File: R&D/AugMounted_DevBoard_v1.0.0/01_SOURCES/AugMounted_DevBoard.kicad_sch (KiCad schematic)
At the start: 1 part

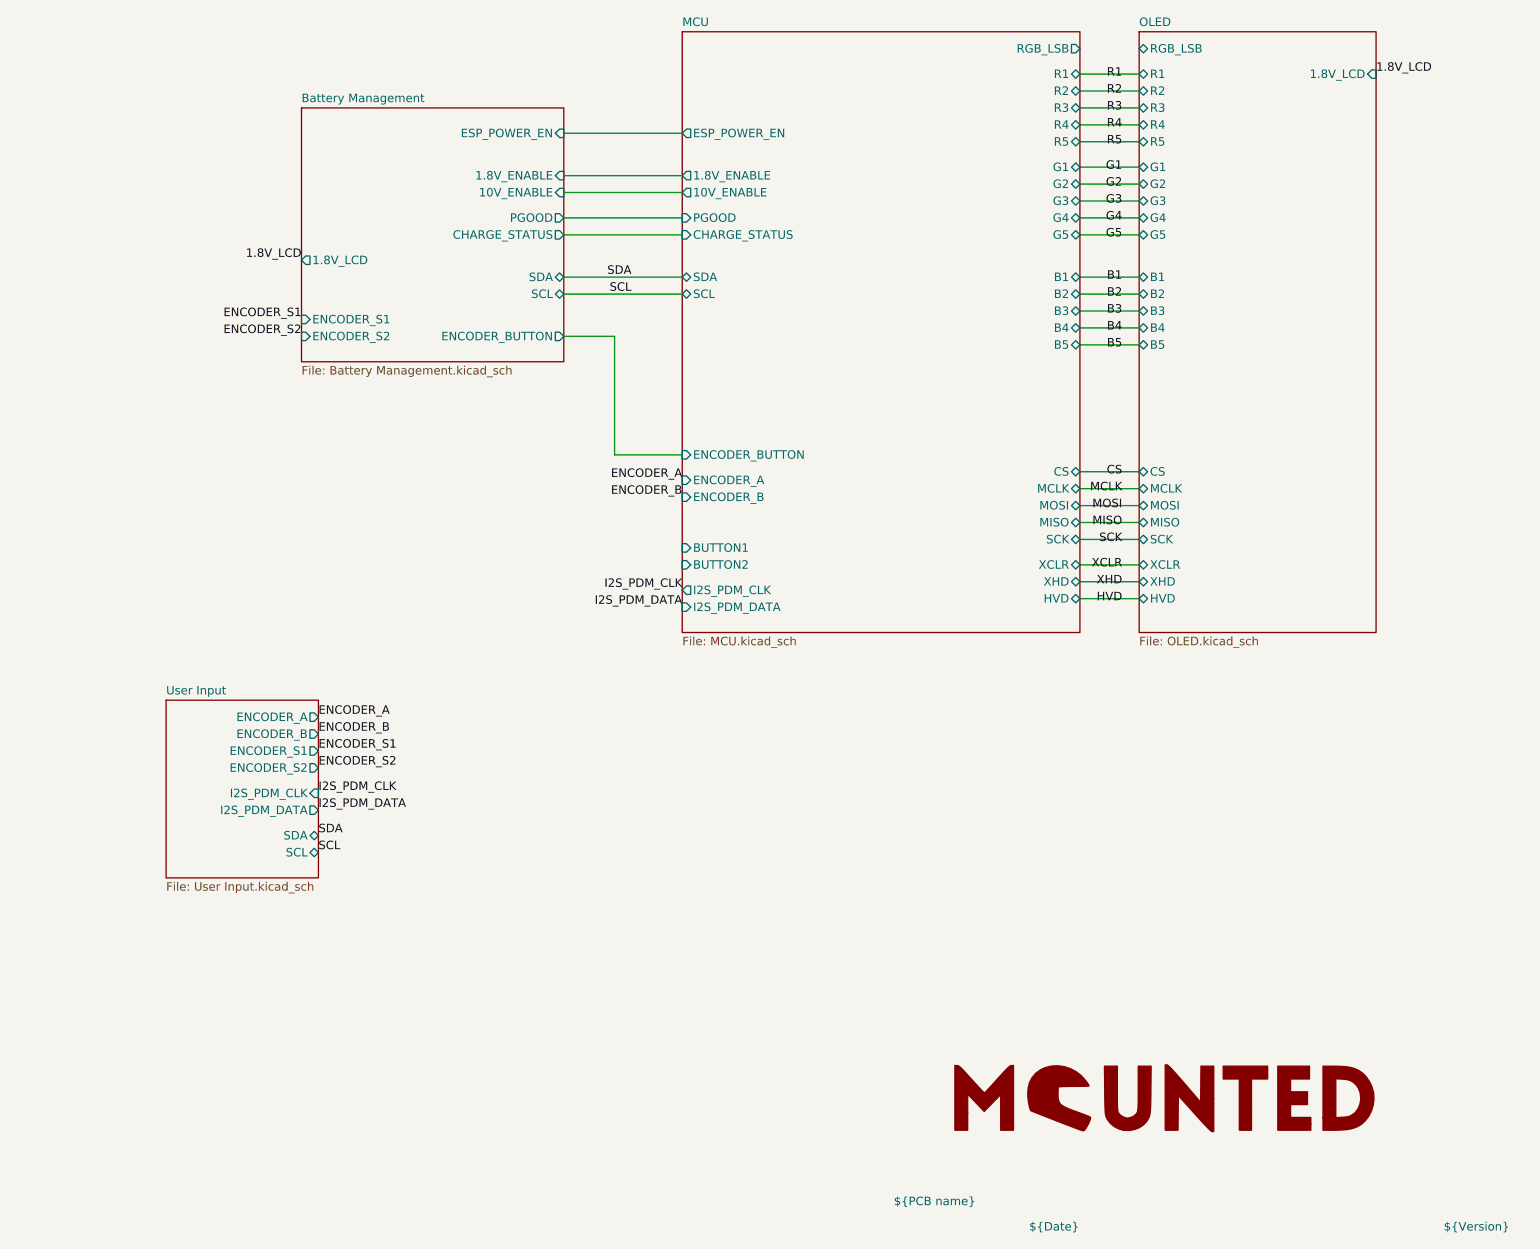
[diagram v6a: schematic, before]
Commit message: Changed layout to a banana shape
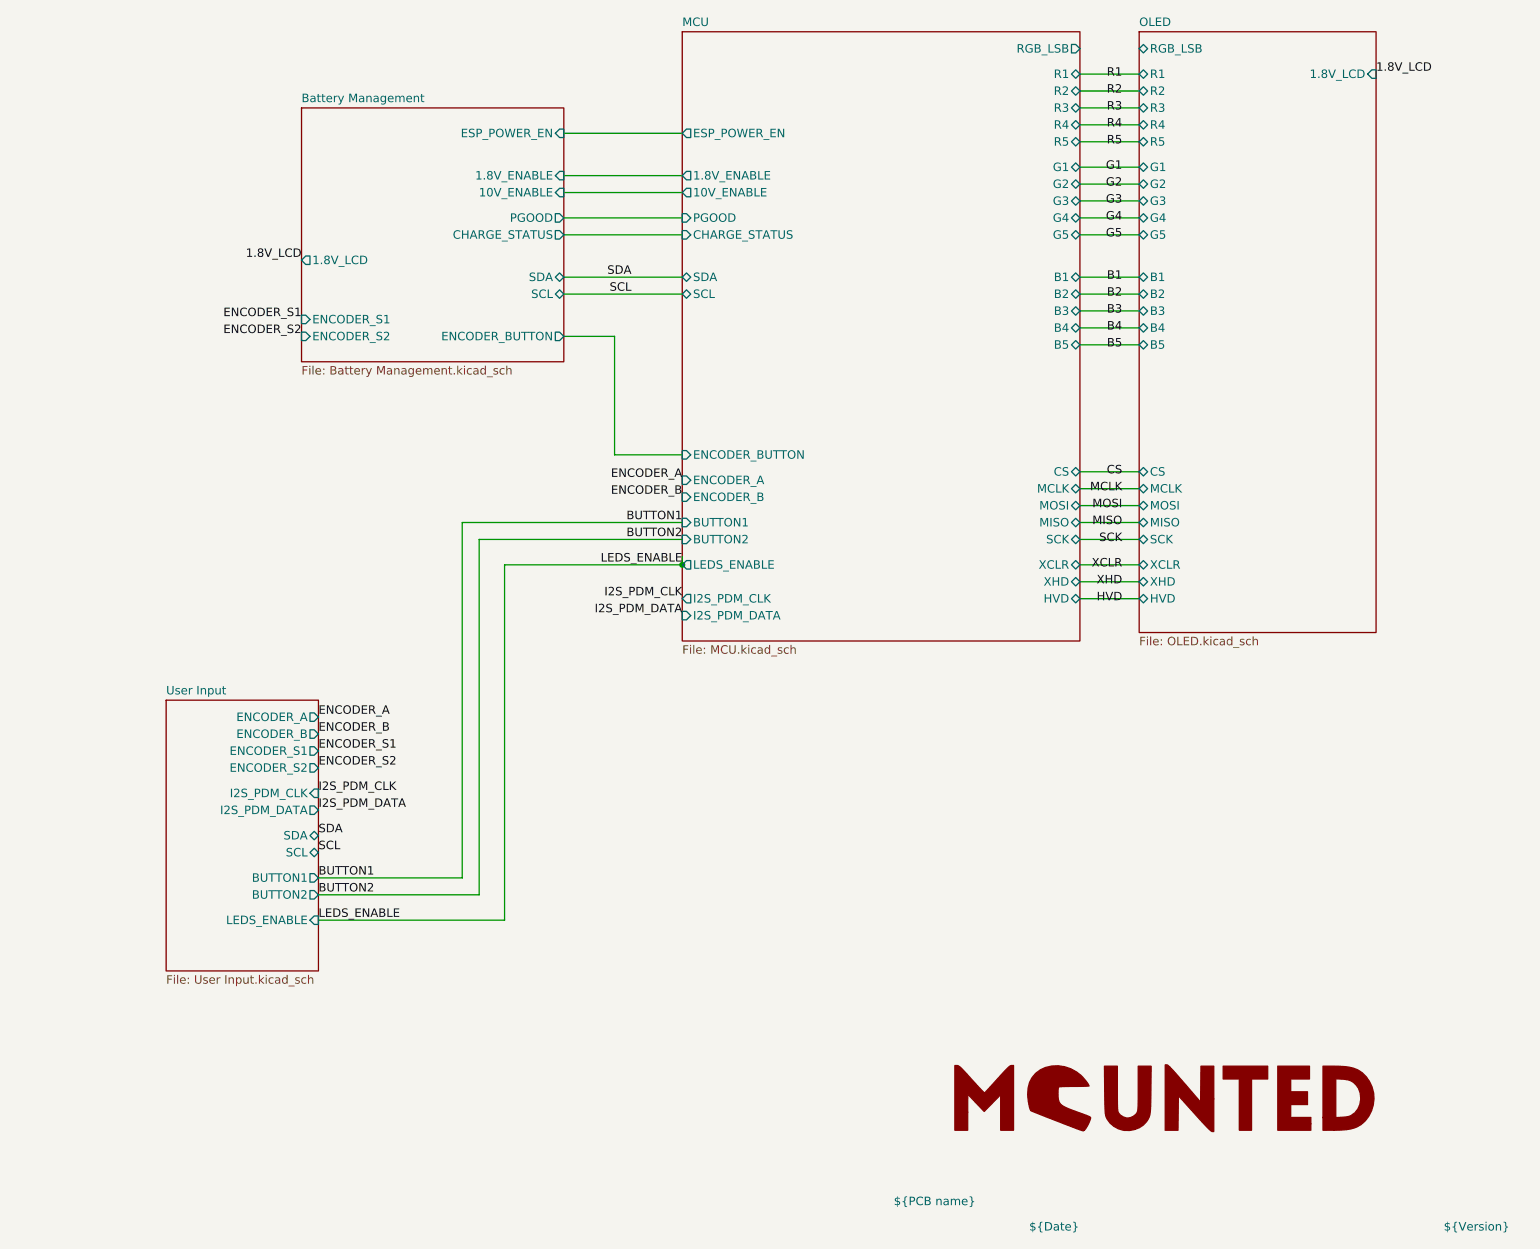
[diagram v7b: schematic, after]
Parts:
- renumbered LOGO1 to LOGO101
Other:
- sheet MCU ports: added LEDS_ENABLE; removed none
- sheet User Input ports: added BUTTON1, BUTTON2, LEDS_ENABLE; removed none
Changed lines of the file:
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@@
 (kicad_sch (version 20230121) (generator eeschema)
   (paper "A4")
+  (junction (at 154.94 93.98) (diameter 0) (color 0 0 0 0)
+  )
   (wire (pts (xy 214.63 55.88) (xy 223.52 55.88))
     (stroke (width 0) (type default))
@@
     (stroke (width 0) (type default))
   )
+  (wire (pts (xy 128.27 93.98) (xy 128.27 147.32))
+    (stroke (width 0) (type default))
+  )
   (wire (pts (xy 214.63 99.06) (xy 223.52 99.06))
     (stroke (width 0) (type default))
@@
     (stroke (width 0) (type default))
   )
+  (wire (pts (xy 154.94 93.98) (xy 128.27 93.98))
+    (stroke (width 0) (type default))
+  )
   (wire (pts (xy 137.16 59.69) (xy 144.78 59.69))
     (stroke (width 0) (type default))
@@
     (stroke (width 0) (type default))
   )
+  (wire (pts (xy 121.92 87.63) (xy 154.94 87.63))
+    (stroke (width 0) (type default))
+  )
   (wire (pts (xy 214.63 87.63) (xy 223.52 87.63))
     (stroke (width 0) (type default))
@@
     (stroke (width 0) (type default))
   )
+  (wire (pts (xy 154.94 93.98) (xy 154.94 92.71))
+    (stroke (width 0) (type default))
+  )
   (wire (pts (xy 214.63 82.55) (xy 223.52 82.55))
     (stroke (width 0) (type default))
@@
     (stroke (width 0) (type default))
   )
+  (wire (pts (xy 100.33 143.51) (xy 124.46 143.51))
+    (stroke (width 0) (type default))
+  )
+  (wire (pts (xy 128.27 147.32) (xy 100.33 147.32))
+    (stroke (width 0) (type default))
+  )
+  (wire (pts (xy 124.46 143.51) (xy 124.46 90.17))
+    (stroke (width 0) (type default))
+  )
   (wire (pts (xy 137.16 44.45) (xy 154.94 44.45))
     (stroke (width 0) (type default))
@@
     (stroke (width 0) (type default))
   )
+  (wire (pts (xy 100.33 140.97) (xy 121.92 140.97))
+    (stroke (width 0) (type default))
+  )
   (wire (pts (xy 144.78 59.69) (xy 144.78 77.47))
     (stroke (width 0) (type default))
@@
     (stroke (width 0) (type default))
   )
+  (wire (pts (xy 121.92 140.97) (xy 121.92 87.63))
+    (stroke (width 0) (type default))
+  )
   (wire (pts (xy 137.16 38.1) (xy 154.94 38.1))
     (stroke (width 0) (type default))
   )
+  (wire (pts (xy 124.46 90.17) (xy 154.94 90.17))
+    (stroke (width 0) (type default))
+  )
   (wire (pts (xy 214.63 41.91) (xy 223.52 41.91))
     (stroke (width 0) (type default))
@@
     (effects (font (size 1.27 1.27)) (justify right))
   )
+  (label "LEDS_ENABLE" (at 154.94 93.98 180) (fields_autoplaced)
+    (effects (font (size 1.27 1.27)) (justify right bottom))
+  )
   (label "ENCODER_S2" (at 97.79 59.69 180) (fields_autoplaced)
     (effects (font (size 1.27 1.27)) (justify right bottom))
@@
     (effects (font (size 1.27 1.27)) (justify right bottom))
   )
-  (label "I2S_PDM_CLK" (at 154.94 97.79 180) (fields_autoplaced)
+  (label "I2S_PDM_CLK" (at 154.94 99.06 180) (fields_autoplaced)
     (effects (font (size 1.27 1.27)) (justify right bottom))
   )
@@
     (effects (font (size 1.27 1.27)) (justify right))
   )
+  (label "BUTTON1" (at 154.94 87.63 180) (fields_autoplaced)
+    (effects (font (size 1.27 1.27)) (justify right bottom))
+  )
   (label "ENCODER_S2" (at 100.33 124.46 0) (fields_autoplaced)
     (effects (font (size 1.27 1.27)) (justify left bottom))
@@
     (effects (font (size 1.27 1.27)) (justify right))
   )
-  (label "I2S_PDM_DATA" (at 154.94 100.33 180) (fields_autoplaced)
-    (effects (font (size 1.27 1.27)) (justify right bottom))
+  (label "I2S_PDM_DATA" (at 154.94 101.6 180) (fields_autoplaced)
+    (effects (font (size 1.27 1.27)) (justify right bottom))
+  )
+  (label "BUTTON1" (at 100.33 140.97 0) (fields_autoplaced)
+    (effects (font (size 1.27 1.27)) (justify left bottom))
   )
   (label "ENCODER_S1" (at 100.33 121.92 0) (fields_autoplaced)
@@
     (effects (font (size 1.27 1.27)) (justify right bottom))
   )
+  (label "LEDS_ENABLE" (at 100.33 147.32 0) (fields_autoplaced)
+    (effects (font (size 1.27 1.27)) (justify left bottom))
+  )
   (label "I2S_PDM_DATA" (at 100.33 130.81 0) (fields_autoplaced)
     (effects (font (size 1.27 1.27)) (justify left bottom))
@@
     (effects (font (size 1.27 1.27)) (justify right bottom))
   )
+  (label "BUTTON2" (at 100.33 143.51 0) (fields_autoplaced)
+    (effects (font (size 1.27 1.27)) (justify left bottom))
+  )
   (label "ENCODER_A" (at 100.33 116.84 0) (fields_autoplaced)
     (effects (font (size 1.27 1.27)) (justify left bottom))
@@
   (label "MCLK" (at 220.98 82.55 180) (fields_autoplaced)
     (effects (font (size 1.27 1.27)) (justify right))
+  )
+  (label "BUTTON2" (at 154.94 90.17 180) (fields_autoplaced)
+    (effects (font (size 1.27 1.27)) (justify right bottom))
   )
   (label "G4" (at 220.98 41.91 180) (fields_autoplaced)
@@
   (symbol (lib_id ".mounted-lib:mounted_logo") (at 227.33 173.99 0) (unit 1)
     (in_bom yes) (on_board yes) (dnp no) (fields_autoplaced)
-    (property "Reference" "LOGO1" (at 227.33 167.64 0)
+    (property "Reference" "LOGO101" (at 227.33 167.64 0)
       (effects (font (size 1.27 1.27)) hide)
     )
@@
       (project "AugMounted_DevBoard"
         (path "/75b08848-9393-425e-a17d-60105119a7b1"
-          (reference "LOGO1") (unit 1)
+          (reference "LOGO101") (unit 1)
         )
       )
     )
   )
-  (sheet (at 77.47 114.3) (size 22.86 26.67) (fields_autoplaced)
+  (sheet (at 77.47 114.3) (size 22.86 40.64) (fields_autoplaced)
     (stroke (width 0.1524) (type solid))
     (fill (color 0 0 0 0.0000))
@@
       (effects (font (size 1.27 1.27)) (justify left bottom))
     )
-    (property "Sheetfile" "User Input.kicad_sch" (at 77.47 141.5546 0)
+    (property "Sheetfile" "User Input.kicad_sch" (at 77.47 155.5246 0)
       (effects (font (size 1.27 1.27)) (justify left top))
     )
@@
     )
     (pin "SCL" bidirectional (at 100.33 137.16 0)
+      (effects (font (size 1.27 1.27)) (justify right))
+    )
+    (pin "BUTTON1" output (at 100.33 140.97 0)
+      (effects (font (size 1.27 1.27)) (justify right))
+    )
+    (pin "BUTTON2" output (at 100.33 143.51 0)
+      (effects (font (size 1.27 1.27)) (justify right))
+    )
+    (pin "LEDS_ENABLE" input (at 100.33 147.32 0)
       (effects (font (size 1.27 1.27)) (justify right))
     )
@@
     )
   )
-  (sheet (at 154.94 13.97) (size 59.69 90.17) (fields_autoplaced)
+  (sheet (at 154.94 13.97) (size 59.69 91.44) (fields_autoplaced)
     (stroke (width 0.1524) (type solid))
     (fill (color 0 0 0 0.0000))
@@
       (effects (font (size 1.27 1.27)) (justify left bottom))
     )
-    (property "Sheetfile" "MCU.kicad_sch" (at 154.94 104.7246 0)
+    (property "Sheetfile" "MCU.kicad_sch" (at 154.94 105.9946 0)
       (effects (font (size 1.27 1.27)) (justify left top))
     )
@@
       (effects (font (size 1.27 1.27)) (justify left))
     )
-    (pin "I2S_PDM_CLK" output (at 154.94 97.79 180)
-      (effects (font (size 1.27 1.27)) (justify left))
-    )
-    (pin "I2S_PDM_DATA" input (at 154.94 100.33 180)
-      (effects (font (size 1.27 1.27)) (justify left))
-    )
-    (pin "BUTTON1" input (at 154.94 91.44 180)
+    (pin "I2S_PDM_CLK" output (at 154.94 99.06 180)
+      (effects (font (size 1.27 1.27)) (justify left))
+    )
+    (pin "I2S_PDM_DATA" input (at 154.94 101.6 180)
+      (effects (font (size 1.27 1.27)) (justify left))
+    )
+    (pin "BUTTON1" input (at 154.94 87.63 180)
       (effects (font (size 1.27 1.27)) (justify left))
     )
@@
       (effects (font (size 1.27 1.27)) (justify left))
     )
-    (pin "BUTTON2" input (at 154.94 93.98 180)
+    (pin "BUTTON2" input (at 154.94 90.17 180)
       (effects (font (size 1.27 1.27)) (justify left))
     )
@@
       (effects (font (size 1.27 1.27)) (justify left))
     )
+    (pin "LEDS_ENABLE" output (at 154.94 93.98 180)
+      (effects (font (size 1.27 1.27)) (justify left))
+    )

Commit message: Added resistors for CC1 and CC2 pins, layout is started on the high part of the board
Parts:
- added H101, H102: MountingHole, MountingHole:MountingHole_2.2mm_M2, symbol Mechanical:MountingHole
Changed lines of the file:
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@@
     (effects (font (size 1.27 1.27)) (justify left bottom))
+  )
+  (symbol (lib_id "Mechanical:MountingHole") (at 229.87 138.43 0) (unit 1)
+    (in_bom yes) (on_board yes) (dnp no) (fields_autoplaced)
+    (property "Reference" "H102" (at 232.41 137.16 0)
+      (effects (font (size 1.27 1.27)) (justify left))
+    )
+    (property "Value" "MountingHole" (at 232.41 139.7 0)
+      (effects (font (size 1.27 1.27)) (justify left))
+    )
+    (property "Footprint" "MountingHole:MountingHole_2.2mm_M2" (at 229.87 138.43 0)
+      (effects (font (size 1.27 1.27)) hide)
+    )
+    (property "Datasheet" "~" (at 229.87 138.43 0)
+      (effects (font (size 1.27 1.27)) hide)
+    )
+    (instances
+      (project "AugMounted_DevBoard"
+        (path "/75b08848-9393-425e-a17d-60105119a7b1"
+          (reference "H102") (unit 1)
+        )
+      )
+    )
   )
   (symbol (lib_id ".mounted-lib:mounted_logo") (at 227.33 173.99 0) (unit 1)
@@
         )
       )
+    )
+  )
+  (symbol (lib_id "Mechanical:MountingHole") (at 209.55 138.43 0) (unit 1)
+    (in_bom yes) (on_board yes) (dnp no) (fields_autoplaced)
+    (property "Reference" "H101" (at 212.09 137.16 0)
+      (effects (font (size 1.27 1.27)) (justify left))
+    )
+    (property "Value" "MountingHole" (at 212.09 139.7 0)
+      (effects (font (size 1.27 1.27)) (justify left))
+    )
+    (property "Footprint" "MountingHole:MountingHole_2.2mm_M2" (at 209.55 138.43 0)
+      (effects (font (size 1.27 1.27)) hide)
+    )
+    (property "Datasheet" "~" (at 209.55 138.43 0)
+      (effects (font (size 1.27 1.27)) hide)
+    )
+    (instances
+      (project "AugMounted_DevBoard"
+        (path "/75b08848-9393-425e-a17d-60105119a7b1"
+          (reference "H101") (unit 1)
+        )
+      )
